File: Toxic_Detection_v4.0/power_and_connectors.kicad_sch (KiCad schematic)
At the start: 40 parts, among them IC3 ESDA6V1U1RL, IC8 TPS2054BDR, IC9 AP7365-33WG-7, J1 DM3AT-SF-PEJM5, J2 Conn_ARM_JTAG_SWD_20, J3 USB_C_Receptacle, J4 Conn_01x04_Pin, J7 Conn_01x04_Pin

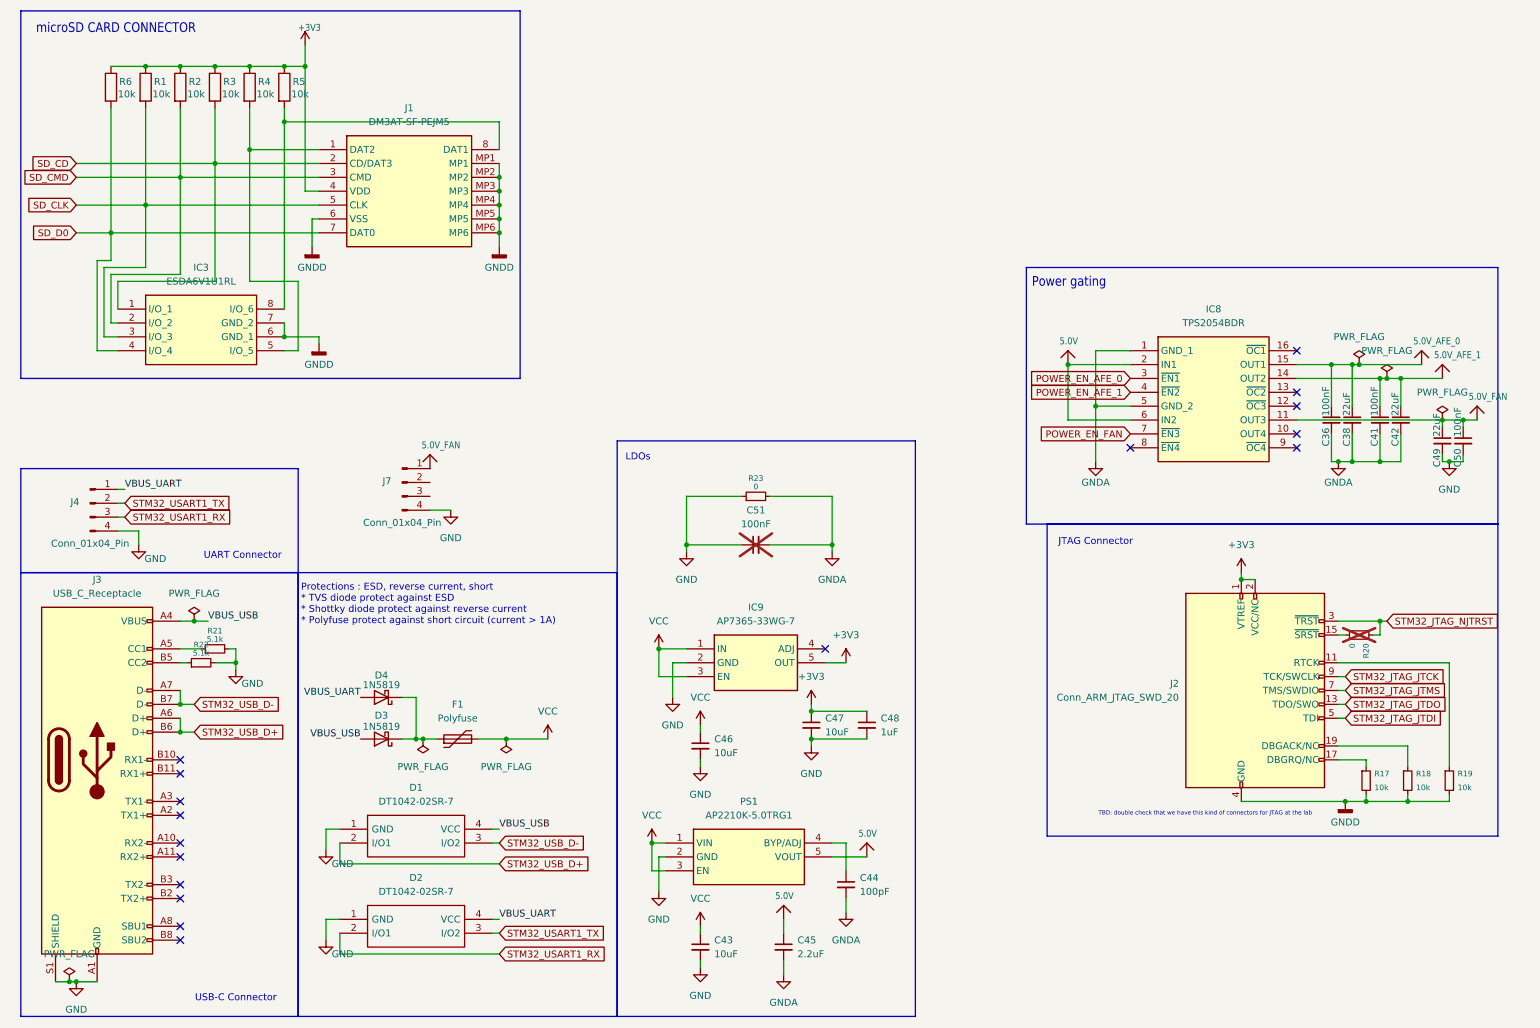
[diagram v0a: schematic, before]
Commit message: feat: add spi between STM32 and ESP32, update JTAG to add ESP32 on it
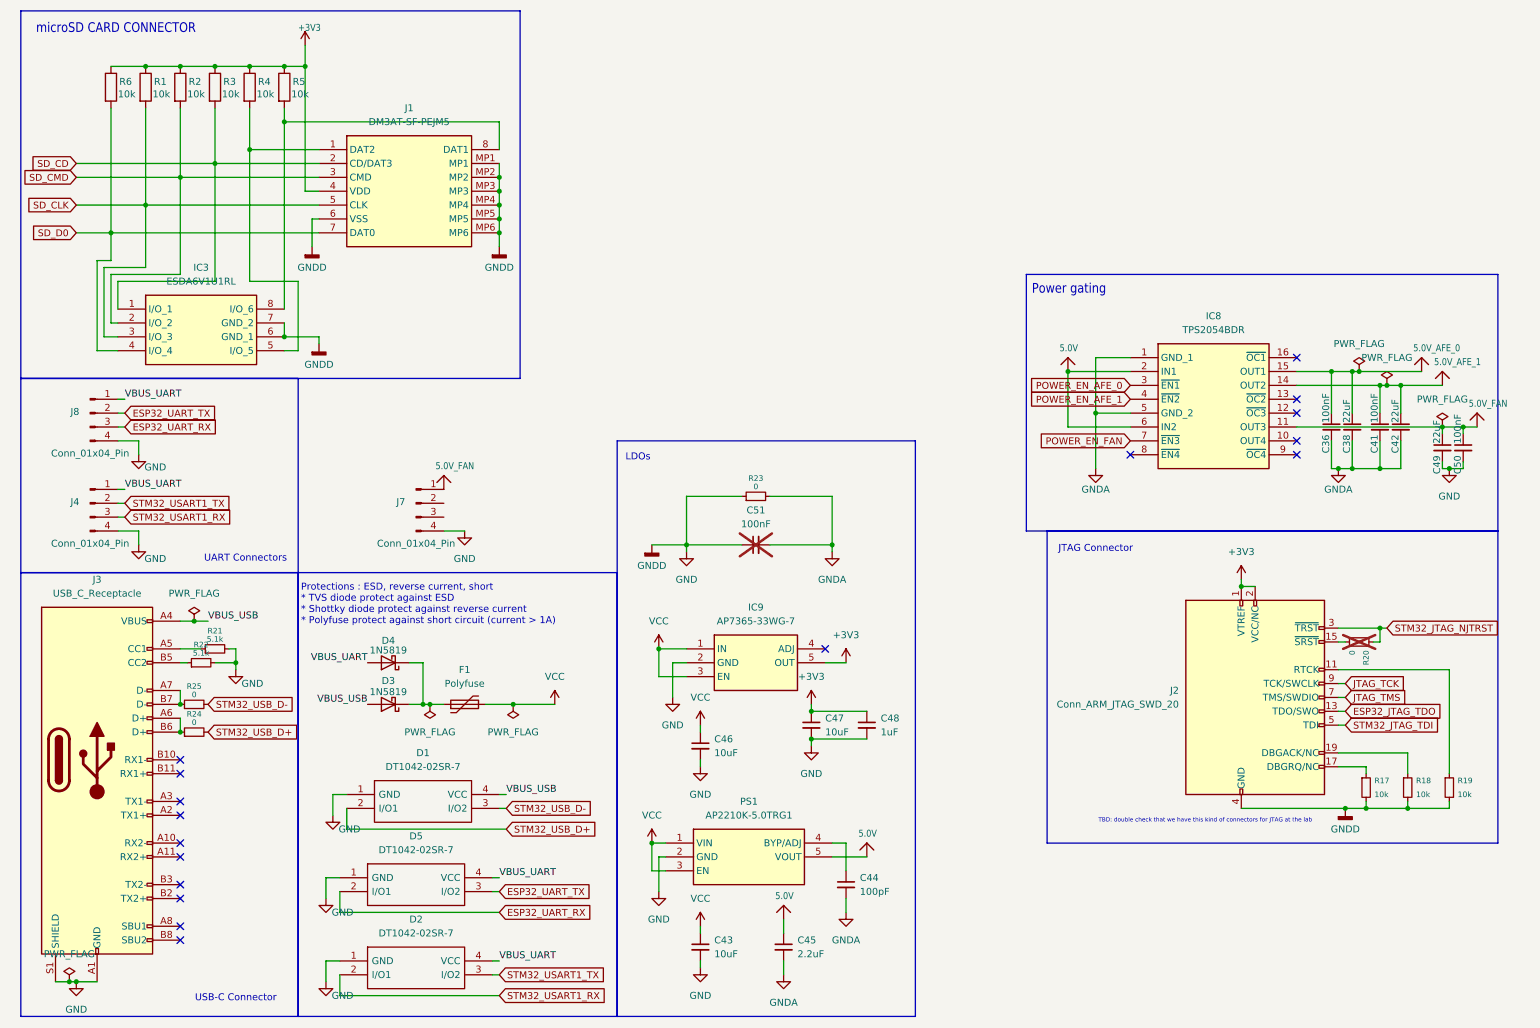
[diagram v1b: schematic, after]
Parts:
- added D5: DT1042-02SR-7, DT104202SR7, symbol DT1042-02SR-7:DT1042-02SR-7
- added J8: Conn_01x04_Pin, symbol Connector:Conn_01x04_Pin
- added R24, R25: 0, symbol Device:R_Small
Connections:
- net GNDD is gone; now on net GND: IC3.6 (GND_1), IC3.7 (GND_2), J1.6 (VSS), J1.MP1, J1.MP2, J1.MP3, J1.MP4, J1.MP5, J1.MP6, J2.10 (GND), J2.12 (GND), J2.14 (GND), J2.16 (GND), J2.18 (GND), J2.20 (GND), J2.4 (GND), J2.6 (GND), J2.8 (GND), R17.2, R18.2, R19.2
- net GND: now also D5.1 (GND), J8.4 (Pin_4)
- net STM32_USB_D+: now also R24.2; no longer J3.A6 (D+), J3.B6 (D+)
- net STM32_USB_D-: now also R25.2; no longer J3.A7 (D-), J3.B7 (D-)
- net VBUS_UART: now also D5.4 (VCC), J8.1 (Pin_1)
- net STM32_JTAG_JTCK renamed JTAG_TCK
- net STM32_JTAG_JTDI renamed STM32_JTAG_TDI
- net STM32_JTAG_JTDO renamed ESP32_JTAG_TDO
- net STM32_JTAG_JTMS renamed JTAG_TMS
- new net: J3.A7 (D-), J3.B7 (D-), R25.1
- new net: J3.A6 (D+), J3.B6 (D+), R24.1
- new net ESP32_UART_RX: D5.2 (I/O1), J8.3 (Pin_3)
- new net ESP32_UART_TX: D5.3 (I/O2), J8.2 (Pin_2)
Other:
- note added: "UART Connectors"
- note removed: "UART Connector"
- moved on the sheet: C36, C38, C41, C42, C49, C50, D1, D2, D3, D4, F1, IC8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

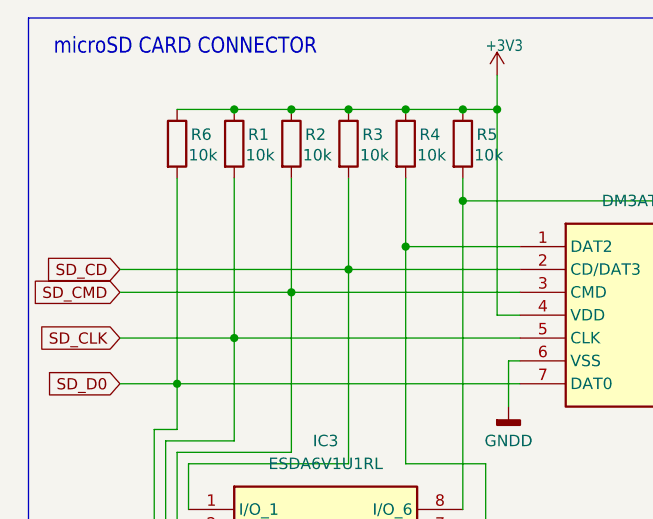
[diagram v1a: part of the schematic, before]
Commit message: feat: add 32MB NOR flash
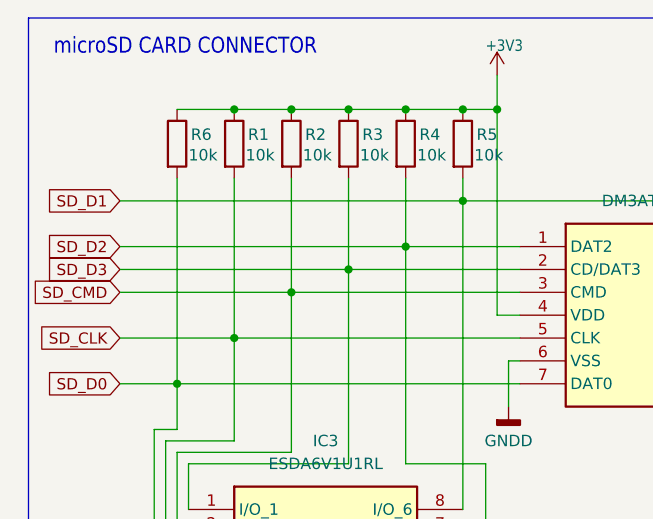
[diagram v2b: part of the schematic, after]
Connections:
- net SD_D2: now reaches IC3.5 (I/O_5), J1.1 (DAT2), R4.2
- net SD_D1: now reaches IC3.8 (I/O_6), J1.8 (DAT1), R5.2
- net SD_CD renamed SD_D3
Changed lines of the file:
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@@
+	(wire
+		(pts
+			(xy 22.86 33.02) (xy 60.96 33.02)
+		)
+		(stroke
+			(width 0)
+			(type default)
+		)
+	)
 	(wire
 		(pts
@@
 		(pts
 			(xy 87.63 139.7) (xy 90.17 139.7)
+		)
+		(stroke
+			(width 0)
+			(type default)
+		)
+	)
+	(wire
+		(pts
+			(xy 22.86 38.1) (xy 54.61 38.1)
 		)
 		(stroke
@@
 		)
 	)
-	(global_label "SD_CD"
+	(global_label "SD_D3"
 		(shape input)
 		(at 22.86 40.64 180)
@@
 		)
 		(property "Intersheetrefs" "${INTERSHEET_REFS}"
-			(at 14.0674 40.64 0)
+			(at 14.1267 40.64 0)
 			(effects
 				(font
@@
 		)
 	)
+	(global_label "SD_D1"
+		(shape input)
+		(at 22.86 33.02 180)
+		(fields_autoplaced yes)
+		(effects
+			(font
+				(size 1.2446 1.2446)
+			)
+			(justify right)
+		)
+		(property "Intersheetrefs" "${INTERSHEET_REFS}"
+			(at 14.1267 33.02 0)
+			(effects
+				(font
+					(size 1.27 1.27)
+				)
+				(justify right)
+				(hide yes)
+			)
+		)
+	)
 	(global_label "STM32_USB_D-"
 		(shape input)
@@
 				(hide yes)
 			)
+		)
+	)
+	(global_label "SD_D2"
+		(shape input)
+		(at 22.86 38.1 180)
+		(fields_autoplaced yes)
+		(effects
+			(font
+				(size 1.2446 1.2446)
+			)
+			(justify right)
+		)
+		(property "Intersheetrefs" "${INTERSHEET_REFS}"
+			(at 14.1267 38.1 0)
+			(effects
+				(font
+					(size 1.27 1.27)
+				)
+				(justify right)
+				(hide yes)
+			)

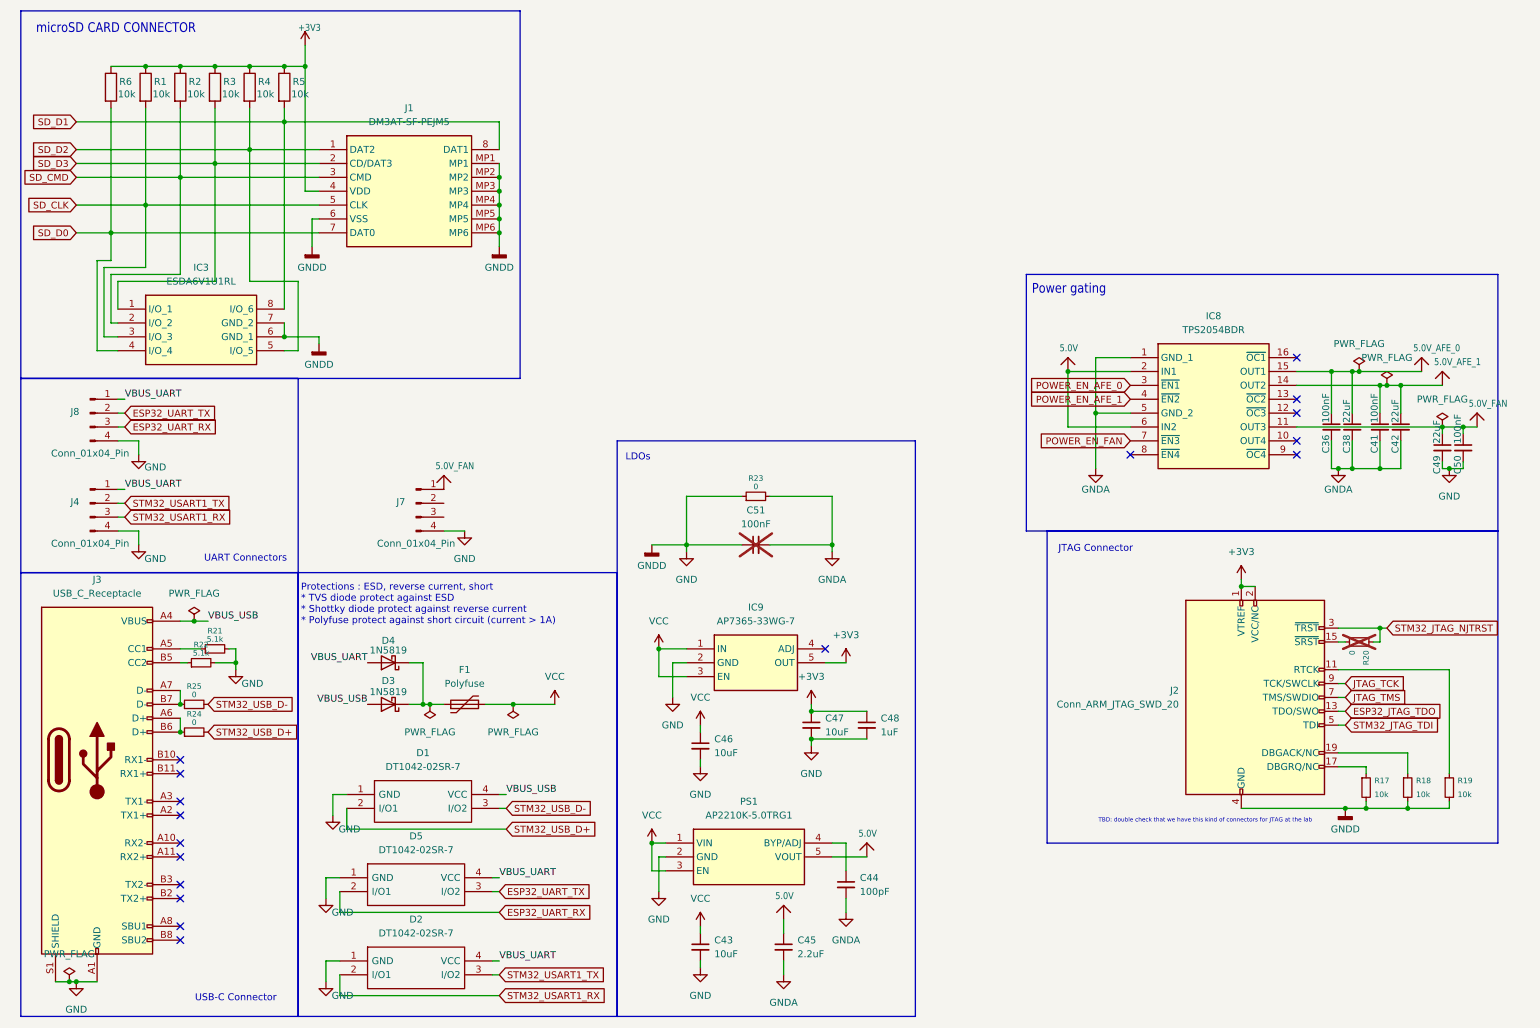
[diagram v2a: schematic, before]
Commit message: feat: add leds and headers
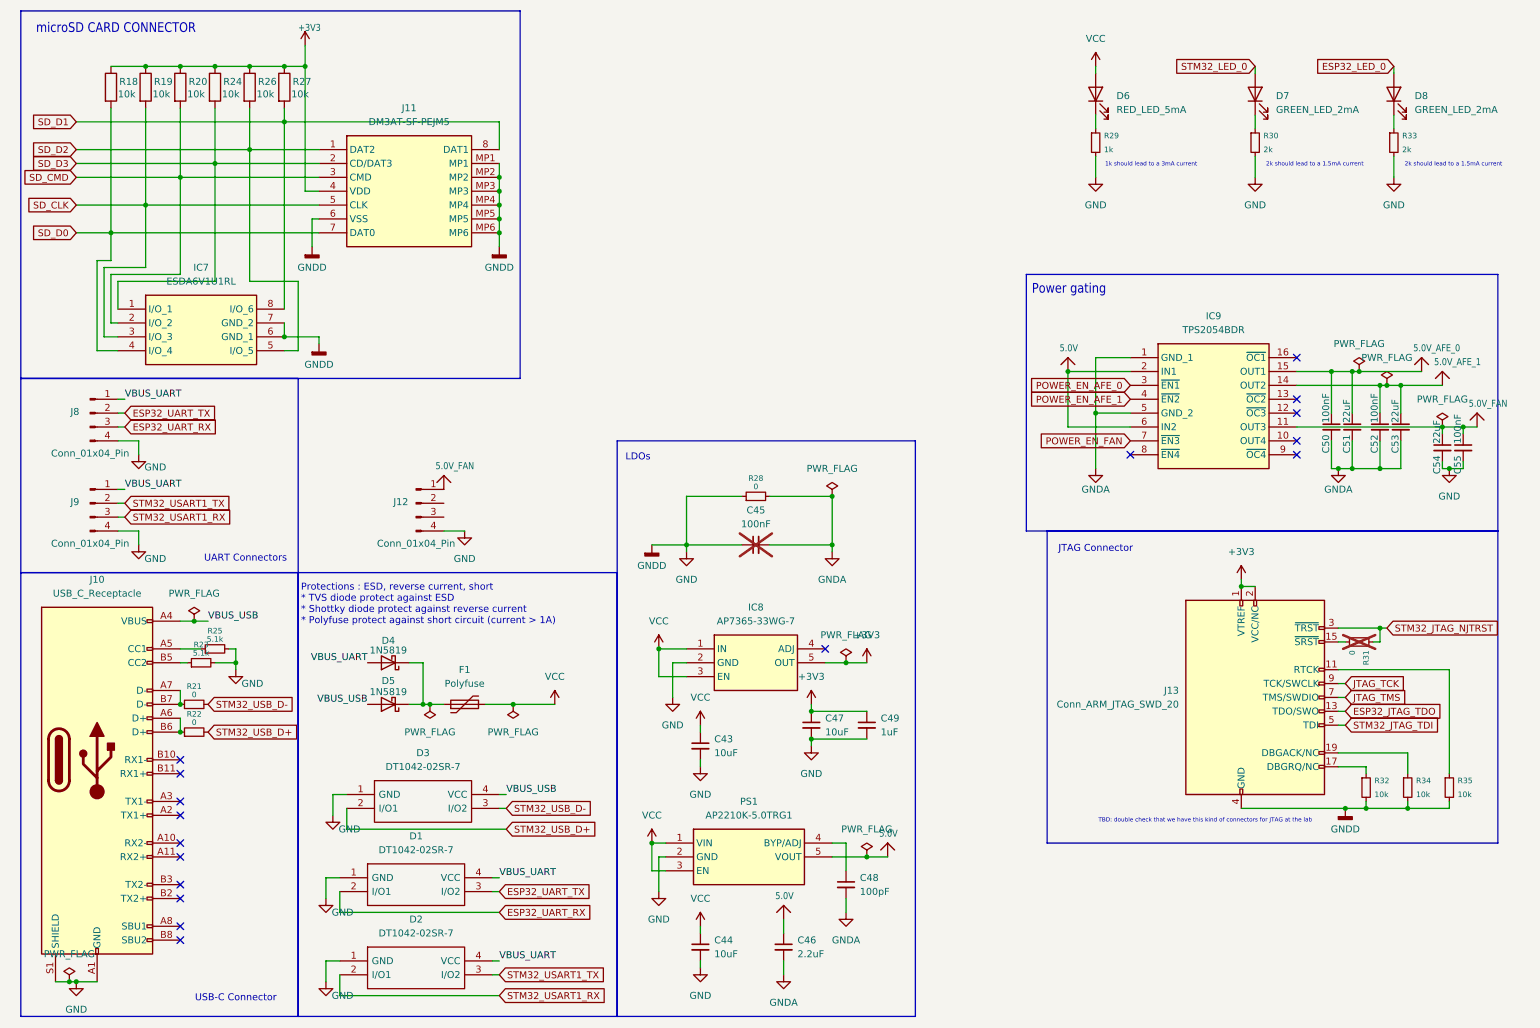
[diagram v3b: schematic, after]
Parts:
- added D6: RED_LED_5mA, symbol Device:LED
- added D7, D8: GREEN_LED_2mA, symbol Device:LED
- added R29: 1k, symbol Device:R_Small
- added R30, R33: 2k, symbol Device:R_Small
- renumbered C46 to C43, C43 to C44, C51 to C45, C45 to C46, C44 to C48, C48 to C49, C36 to C50, C38 to C51, C41 to C52, C42 to C53, C49 to C54, C50 to C55, D5 to D1, D1 to D3, D3 to D5, IC3 to IC7, IC9 to IC8, IC8 to IC9, J3 to J10, J1 to J11, J7 to J12, J2 to J13, J4 to J9, R6 to R18, R1 to R19, R2 to R20, R25 to R21, R24 to R22, R22 to R23, R3 to R24, R21 to R25, R4 to R26, R5 to R27, R23 to R28, R20 to R31, R17 to R32, R18 to R34, R19 to R35
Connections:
- net GND: now also R29.2, R30.2, R33.2
- net VCC: now also D6.2 (A)
- new net: D6.1 (K), R29.1
- new net: D8.1 (K), R33.1
- new net: D7.1 (K), R30.1
- new net ESP32_LED_0: D8.2 (A)
- new net STM32_LED_0: D7.2 (A)
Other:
- note added: "1k should lead to a 3mA current"
- note added: "2k should lead to a 1.5mA current"

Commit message: feat: assign footprints and pass ERC
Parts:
- C42: renamed from C43; footprint (none) -> Capacitor_SMD:C_0805_2012Metric_Pad1.18x1.45mm_HandSolder
- C43: renamed from C44; footprint (none) -> Capacitor_SMD:C_0805_2012Metric_Pad1.18x1.45mm_HandSolder
- C44: renamed from C45; footprint (none) -> Capacitor_SMD:C_0805_2012Metric_Pad1.18x1.45mm_HandSolder
- C45: renamed from C46; footprint (none) -> Capacitor_SMD:C_0805_2012Metric_Pad1.18x1.45mm_HandSolder
- C46: renamed from C47; footprint (none) -> Capacitor_SMD:C_0805_2012Metric_Pad1.18x1.45mm_HandSolder
- C47: renamed from C48; footprint (none) -> Capacitor_SMD:C_0805_2012Metric_Pad1.18x1.45mm_HandSolder
- C48: renamed from C49; footprint (none) -> Capacitor_SMD:C_0805_2012Metric_Pad1.18x1.45mm_HandSolder
- C49: renamed from C50; footprint (none) -> Capacitor_SMD:C_0805_2012Metric_Pad1.18x1.45mm_HandSolder
- C50: renamed from C51; footprint (none) -> Capacitor_SMD:C_0805_2012Metric_Pad1.18x1.45mm_HandSolder
- C51: renamed from C52; footprint (none) -> Capacitor_SMD:C_0805_2012Metric_Pad1.18x1.45mm_HandSolder
- C52: renamed from C53; footprint (none) -> Capacitor_SMD:C_0805_2012Metric_Pad1.18x1.45mm_HandSolder
- C53: renamed from C54; footprint (none) -> Capacitor_SMD:C_0805_2012Metric_Pad1.18x1.45mm_HandSolder
- C54: renamed from C55; footprint (none) -> Capacitor_SMD:C_0805_2012Metric_Pad1.18x1.45mm_HandSolder
- D1, D2, D3: footprint DT104202SR7 -> USB_ESD_protection:DT104202SR7
- D6, D7, D8: footprint (none) -> LED Green:LEDC2012X120N
- IC7: footprint SOIC127P600X175-8N -> TVS_diodes:SOIC127P600X175-8N
- IC8: footprint SOT95P285X130-5N -> LDO 3.3V:SOT95P285X130-5N
- IC9: footprint SOIC127P600X175-16N -> Power Gating TPS2054BDR:SOIC127P600X175-16N
- J10: footprint (none) -> Connector_USB:USB_C_Receptacle_GCT_USB4105-xx-A_16P_TopMnt_Horizontal
- J11: footprint DM3ATSFPEJM5 -> SD card holder:DM3ATSFPEJM5
- J12: footprint (none) -> Connector_PinSocket_2.54mm:PinSocket_1x04_P2.54mm_Vertical
- J13: footprint (none) -> Connector_PinSocket_2.54mm:PinSocket_2x10_P2.54mm_Vertical
- J8, J9: footprint (none) -> Connector_PinHeader_2.54mm:PinHeader_1x04_P2.54mm_Vertical
- PS1: footprint SOT95P282X145-5N -> LDO 5V:SOT95P282X145-5N
- R18, R19, R20, R21, R22, R23, R24, R25, R26, R27, R28, R29, R30, R31, R32, R33, R34, R35: footprint (none) -> Resistor_SMD:R_0805_2012Metric_Pad1.20x1.40mm_HandSolder
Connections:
- net 5.0V renamed +5V
- net 5.0V_AFE_0 renamed +5V_AFE_0
- net 5.0V_AFE_1 renamed +5V_AFE_1
- net 5.0V_FAN renamed +5V_FAN
- no-connect marks 17 -> 19
